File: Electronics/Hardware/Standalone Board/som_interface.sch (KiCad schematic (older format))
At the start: 1 part, among them J1 2309411-2

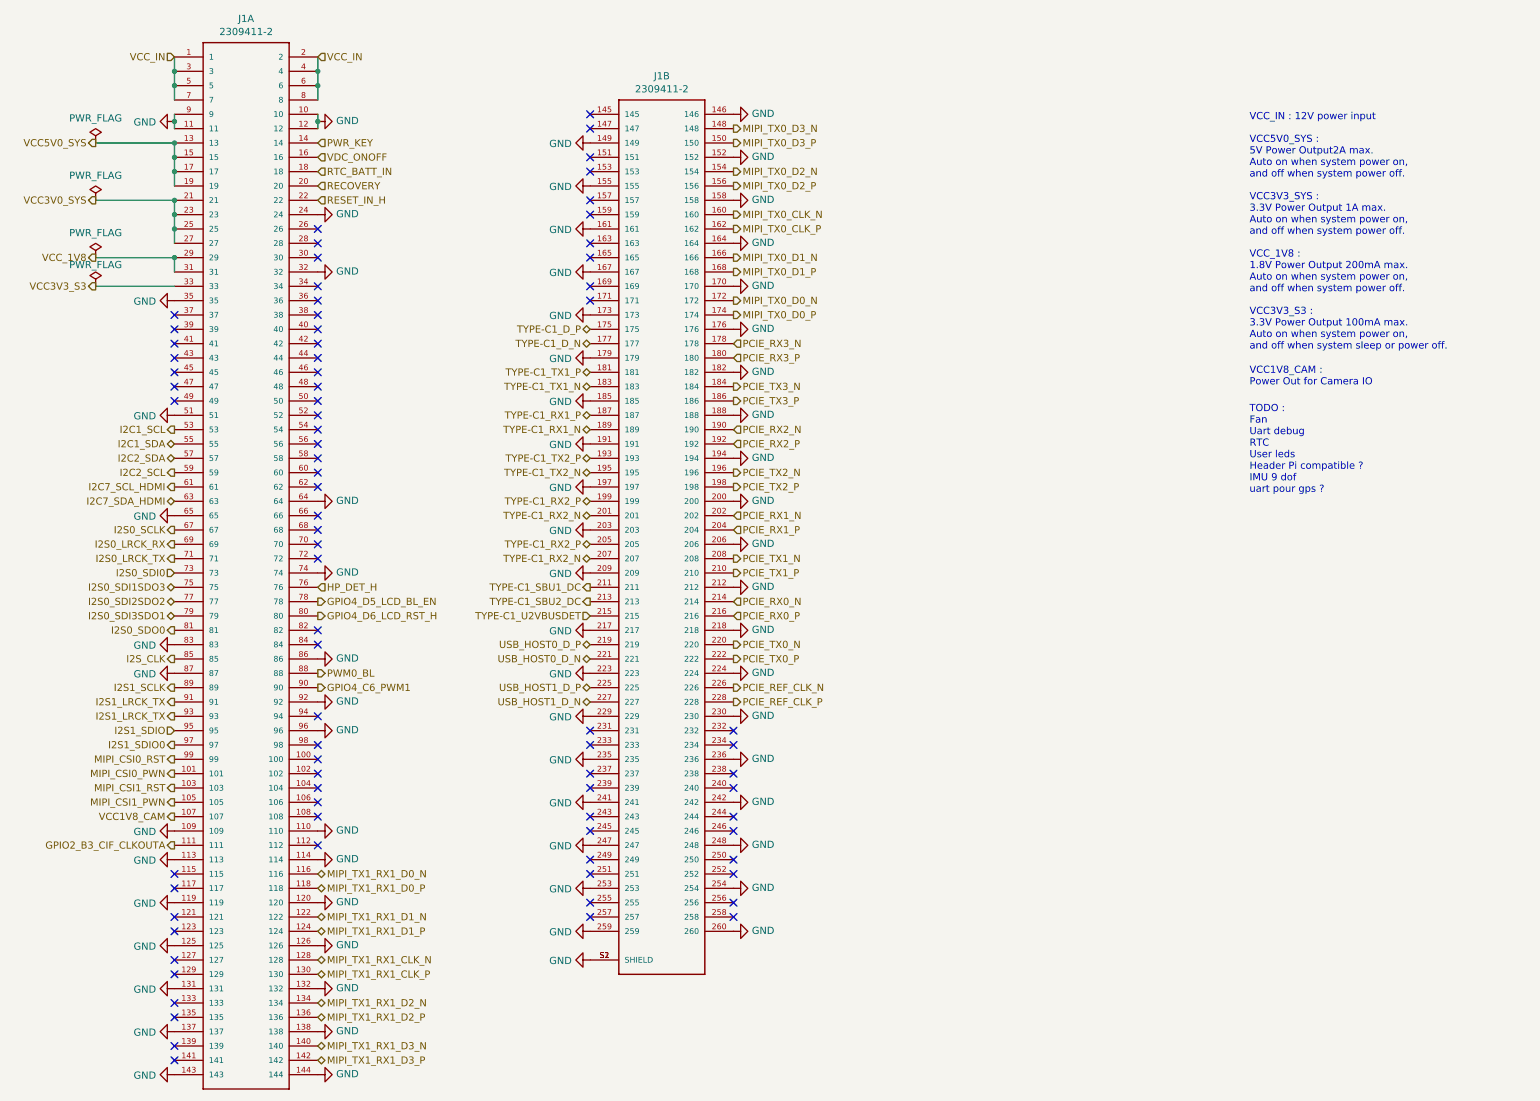
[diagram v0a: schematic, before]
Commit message: Add debug uart, gps uart, fan control and sdcard
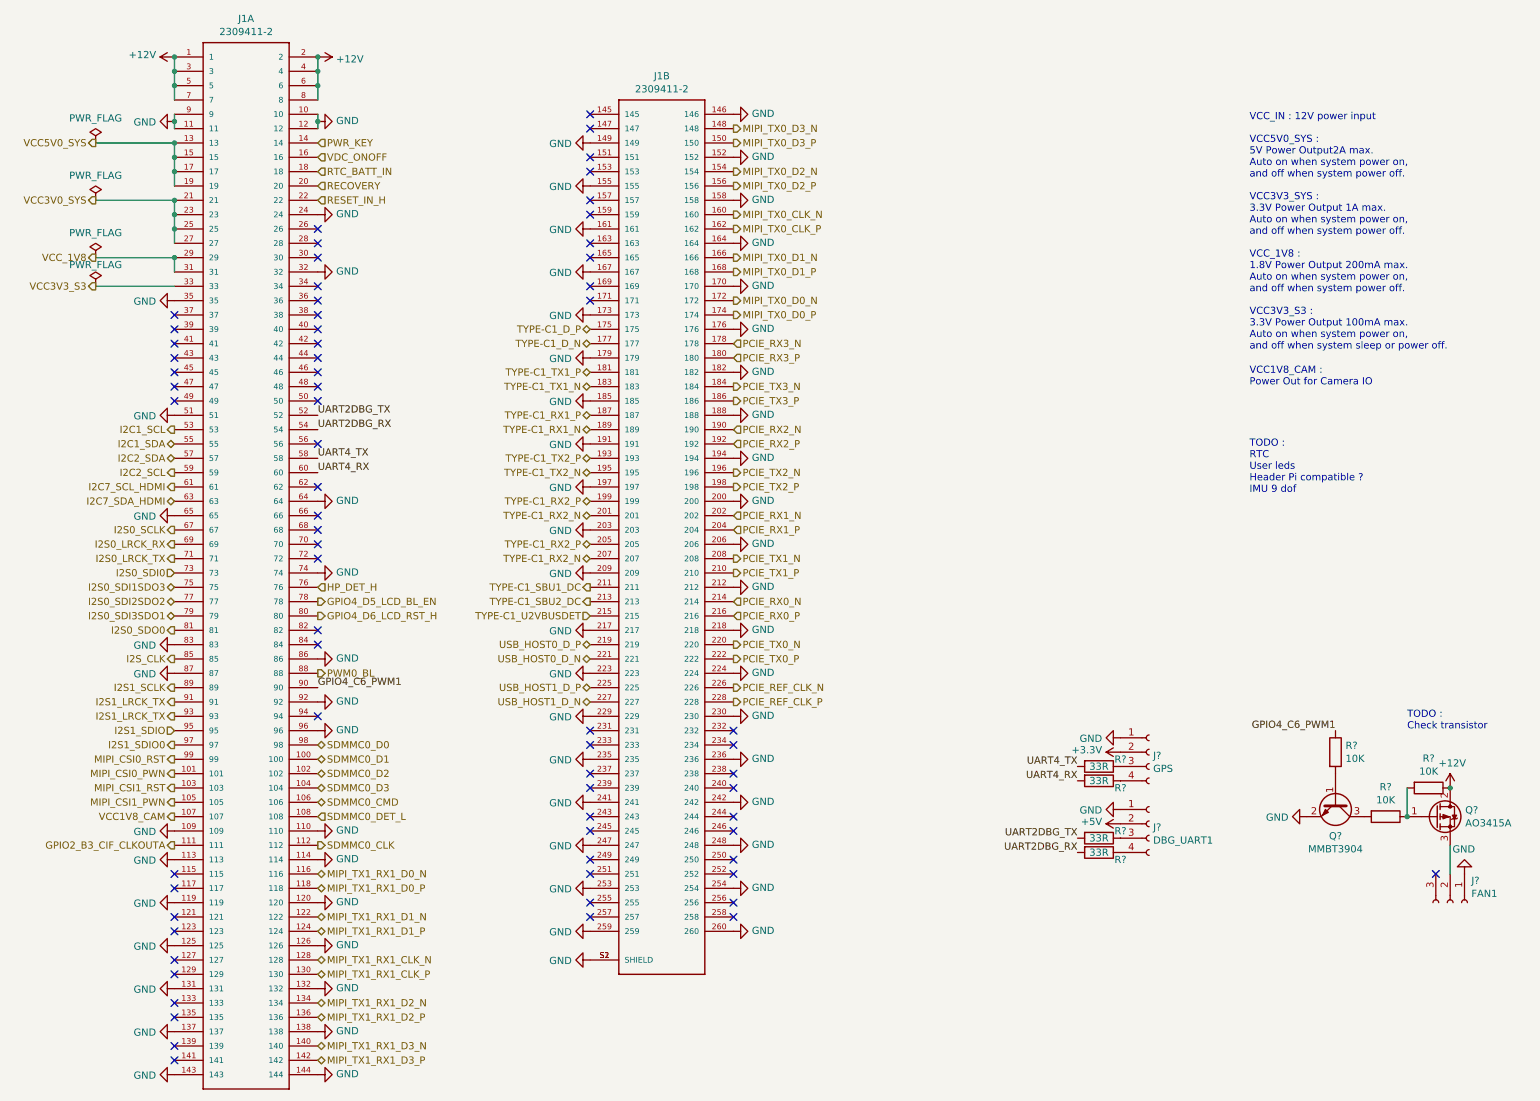
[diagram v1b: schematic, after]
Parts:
- added J?: FAN1, symbol Connector:Conn_01x03_Female
- added J?: DBG_UART1, symbol Connector:Conn_01x04_Female
- added J?: GPS, symbol Connector:Conn_01x04_Female
- added Q?: AO3415A, symbol Device:Q_PMOS_GDS
- added Q?: MMBT3904, Package_TO_SOT_SMD:SOT-23, symbol Transistor_BJT:MMBT3904
- added R? (x3): 10K, symbol Device:R
- added R? (x4): 33R, symbol Device:R
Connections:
- net GND: now also J?.1 (Pin_1), J?.1 (Pin_1), J?.1 (Pin_1), Q?.2 (E)
- net GPIO4_C6_PWM1: now also R?.1
- net SDMMC0_D1: now reaches J1.100
- net SDMMC0_D2: now reaches J1.102
- net SDMMC0_D3: now reaches J1.104
- net SDMMC0_CMD: now reaches J1.106
- net SDMMC0_DET_L: now reaches J1.108
- net SDMMC0_CLK: now reaches J1.112
- net UART2DBG_TX: now reaches J1.52
- net UART2DBG_TX: now also R?.2
- net UART2DBG_RX: now reaches J1.54
- net UART2DBG_RX: now also R?.2
- net UART4_TX: now reaches J1.58
- net UART4_TX: now also R?.2
- net UART4_RX: now reaches J1.60
- net UART4_RX: now also R?.2
- net SDMMC0_D0: now reaches J1.98
- net VCC_IN renamed +12V
- net +12V: now also Q?.2 (D), R?.1
- new net: Q?.1 (G), R?.1, R?.2
- new net: J?.2 (Pin_2), Q?.3 (S)
- new net: Q?.1 (B), R?.2
- new net: Q?.3 (C), R?.2
- new net: J?.3 (Pin_3), R?.1 (x2)
- new net: J?.4 (Pin_4), R?.1 (x2)
- new net +3V3: J?.2 (Pin_2)
- new net +5V: J?.2 (Pin_2)
- no-connect marks 79 -> 69
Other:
- note added: "TODO : \nCheck transistor"
- note added: "TODO :\nRTC\nUser leds\nHeader Pi compatible ?\nIMU 9 dof"
- note removed: "TODO :\nFan\nUart debug\nRTC\nUser leds\nHeader Pi compatible ?\nIMU 9 dof\nuart pour gps ?"

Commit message: Add rtc, pcie + mipi dsi high level connection, usb 2.0, usb 3.0 and remove audio section
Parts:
- added BT?: Battery_Cell, symbol Device:Battery_Cell
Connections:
- net GND: now also BT?.2 (-)
- net RTC_BATT_IN: now also BT?.1 (+)
- net I2C7_SCL_HDMI: no longer names the net of J1.61
- net I2C7_SDA_HDMI: no longer names the net of J1.63
- no-connect marks 69 -> 71
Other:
- note added: "TODO :\nUser leds\nHeader Pi compatible ?\nIMU 9 dof"
- note removed: "TODO :\nRTC\nUser leds\nHeader Pi compatible ?\nIMU 9 dof"
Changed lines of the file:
@@
 EESchema Schematic File Version 4
-LIBS:Standalone Board-cache
 EELAYER 30 0
 EELAYER END
 $Descr A4 11693 8268
 encoding utf-8
-Sheet 2 7
+Sheet 2 6
 Title ""
 Date ""
@@
 Text HLabel 1800 3400 0    50   BiDi ~ 0
 I2C2_SDA
-Text HLabel 1800 3600 0    50   Output ~ 0
-I2C7_SCL_HDMI
-Text HLabel 1800 3700 0    50   BiDi ~ 0
-I2C7_SDA_HDMI
 $Comp
 L power:GND #PWR?
@@
 Text HLabel 2800 1300 2    50   Input ~ 0
 VDC_ONOFF
-Text HLabel 2800 1400 2    50   Input ~ 0
-RTC_BATT_IN
 Text HLabel 2800 1500 2    50   Input ~ 0
 RECOVERY
@@
 NoConn ~ 2800 5200
 Text Notes 9300 3650 0    50   ~ 0
-TODO :\nRTC\nUser leds\nHeader Pi compatible ?\nIMU 9 dof
+TODO :\nUser leds\nHeader Pi compatible ?\nIMU 9 dof
 NoConn ~ 2800 1800
 NoConn ~ 2800 1900
@@
 Text HLabel 2800 6100 2    50   Output ~ 0
 SDMMC0_CLK
+NoConn ~ 1800 3600
+NoConn ~ 1800 3700
+Text Label 2800 1400 0    50   ~ 0
+RTC_BATT_IN
+Text Label 10550 4300 2    50   ~ 0
+RTC_BATT_IN
+$Comp
+L Device:Battery_Cell BT?
+U 1 1 5DF5D410
+P 10550 4500
+F 0 "BT?" H 10668 4596 50  0000 L CNN
+F 1 "Battery_Cell" H 10668 4505 50  0000 L CNN
+F 2 "" V 10550 4560 50  0001 C CNN
+F 3 "~" V 10550 4560 50  0001 C CNN
+	1    10550 4500
+	1    0    0    -1
+$EndComp
+$Comp
+L power:GND #PWR?
+U 1 1 5DF698CD
+P 10550 4600
+F 0 "#PWR?" H 10550 4350 50  0001 C CNN
+F 1 "GND" H 10555 4427 50  0000 C CNN
+F 2 "" H 10550 4600 50  0001 C CNN
+F 3 "" H 10550 4600 50  0001 C CNN
+	1    10550 4600
+	1    0    0    -1
+$EndComp
 $EndSCHEMATC

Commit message: Fix all i2c voltage, add power/reset/recovery button, Mipi dsi hig level, add 3.0/3.3/5/1.1 volt power rail
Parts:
- removed J?: GPS, symbol Connector:Conn_01x04_Female
- removed R? (x2): 33R, symbol Device:R
- added J?: GPIO, symbol Connector:Conn_01x12_Female
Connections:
- net +3V3: now also J?.4 (Pin_4)
- net +5V: now also J?.2 (Pin_2)
- net GND: now also J?.1 (Pin_1), J?.3 (Pin_3)
- net UART4_RX: now also J?.6 (Pin_6)
- net UART4_TX: now also J?.5 (Pin_5)
- net GPIO2_A2: now reaches J1.39
- net GPIO2_A3: now reaches J1.41
- net GPIO1_C2: now reaches J1.42
- net GPIO1_C2: now also J?.9 (Pin_9)
- net GPIO1_C6: now reaches J1.44
- net GPIO1_C6: now also J?.10 (Pin_10)
- net GPIO1_C7: now reaches J1.46
- net GPIO1_C7: now also J?.11 (Pin_11)
- net GPIO1_D0: now reaches J1.48
- net GPIO1_D0: now also J?.12 (Pin_12)
- net GPIO4_C1_I2C3_SCL: now reaches J1.66
- net GPIO4_C1_I2C3_SCL: now also J?.7 (Pin_7)
- net GPIO4_C0_I2C3_SDA: now reaches J1.68
- net GPIO4_C0_I2C3_SDA: now also J?.8 (Pin_8)
- net VCC3V0_SD: now reaches J1.94
- net VCC3V0_SYS renamed VCC3V3_SYS
- no-connect marks 71 -> 62
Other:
- note added: "TODO :\nUser leds"
- note removed: "TODO :\nUser leds\nHeader Pi compatible ?\nIMU 9 dof"
- moved on the sheet: BT?, J?, Q?, R?

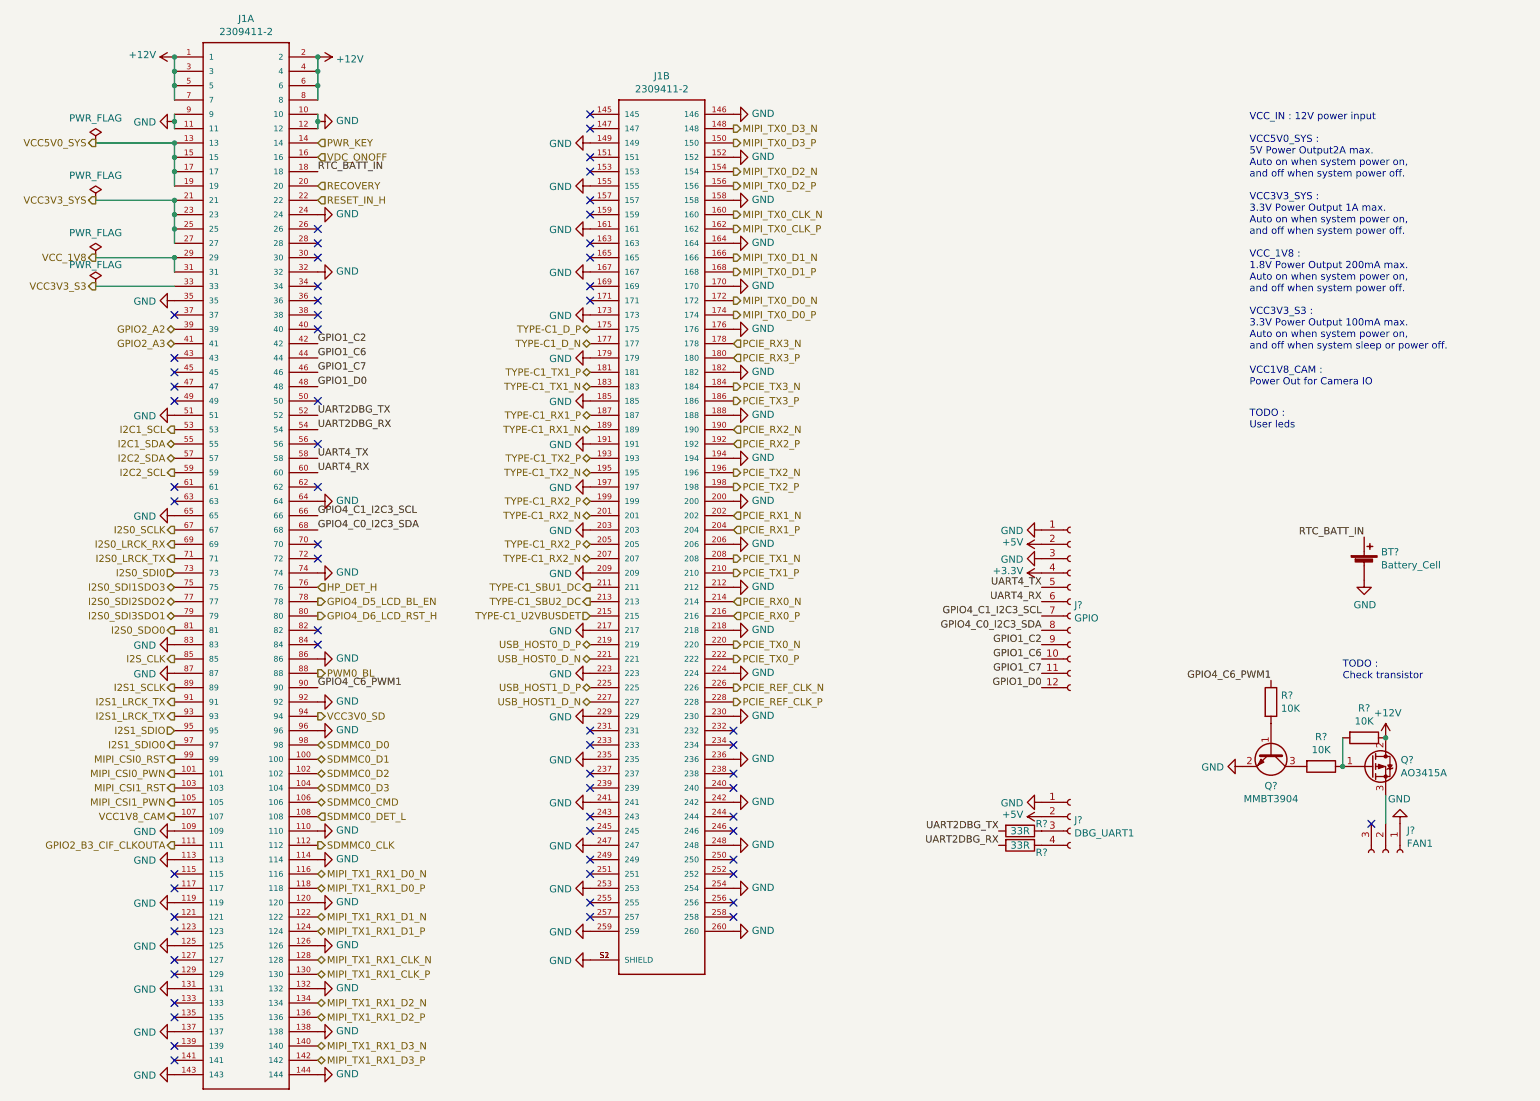
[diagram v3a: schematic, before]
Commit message: Everything is routed, TODO : lenghtmatching + impedance matching + cleaning
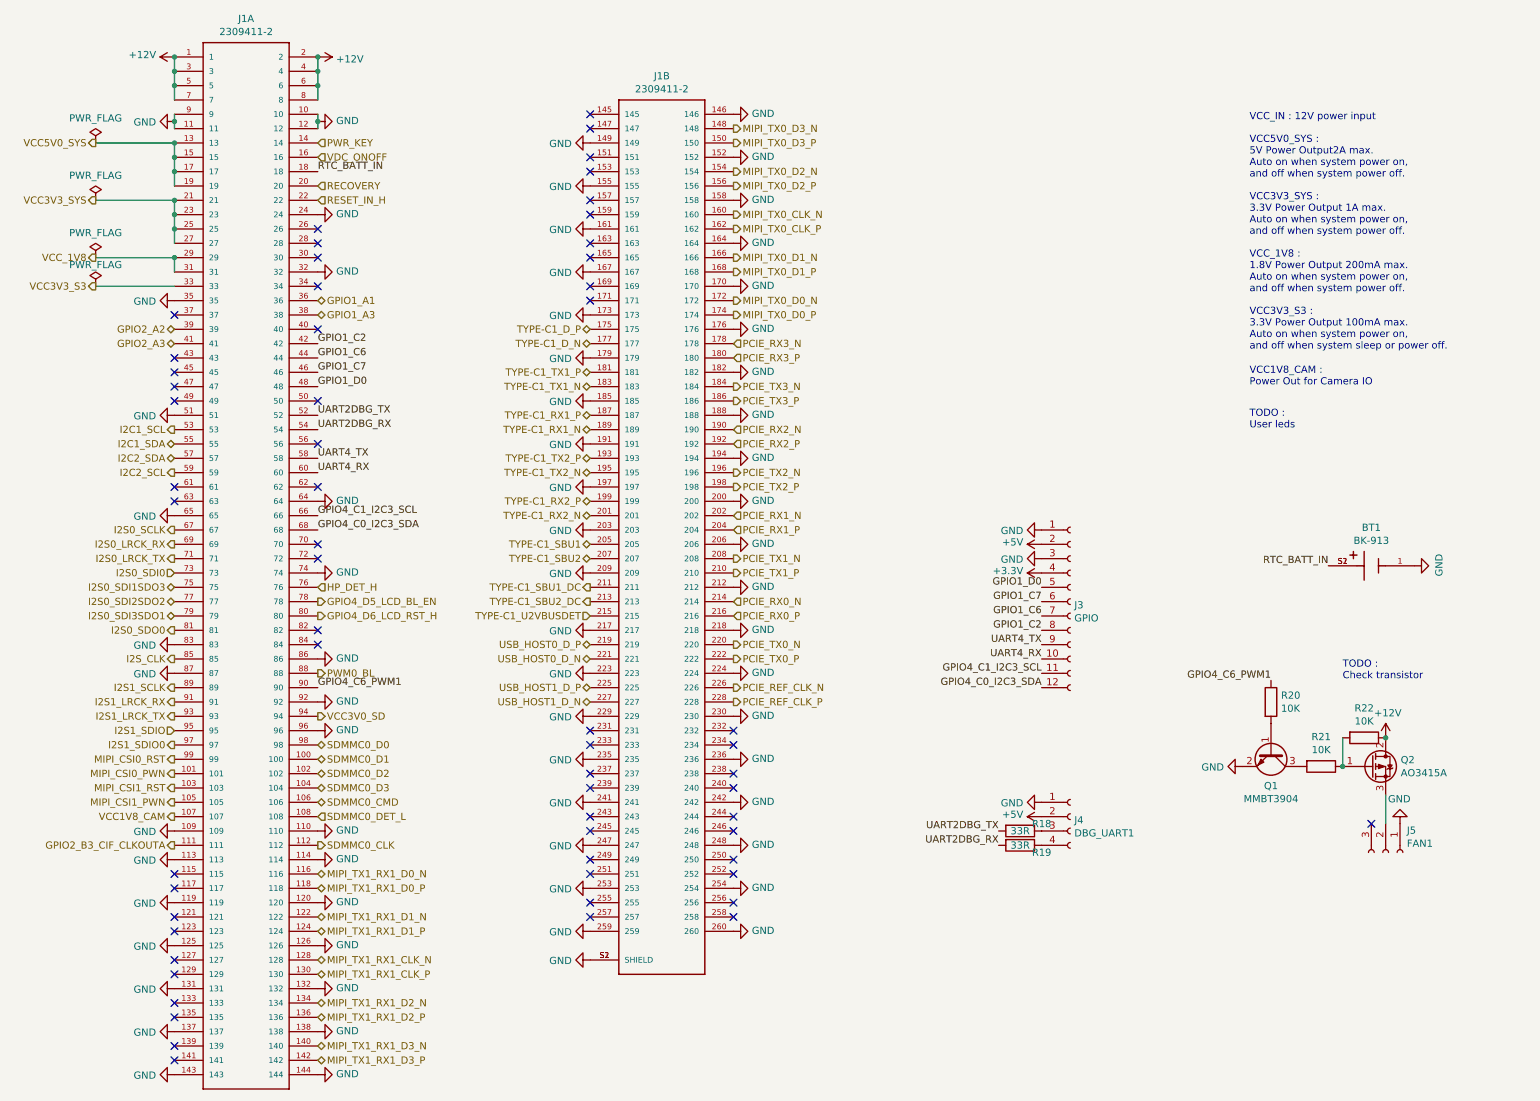
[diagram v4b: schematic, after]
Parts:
- removed BT?: Battery_Cell, symbol Device:Battery_Cell
- added BT1: BK-913, BK-913:BAT_BK-913, symbol BK-913:BK-913
- J3: renamed from J?; footprint (none) -> Connector_PinHeader_1.00mm:PinHeader_1x12_P1.00mm_Vertical
- J4: renamed from J?; footprint (none) -> Connector_PinHeader_1.00mm:PinHeader_1x04_P1.00mm_Vertical
- J5: renamed from J?; footprint (none) -> Connector_PinHeader_1.00mm:PinHeader_1x03_P1.00mm_Vertical
- Q2: renamed from Q?; footprint (none) -> Package_TO_SOT_SMD:SOT-23
- R18, R19, R20, R21, R22: renamed from R?; footprint (none) -> Resistor_SMD:R_0201_0603Metric
- gave numbers to parts that had none: 1
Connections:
- net GND: now also BT1.1 (-)
- net GPIO1_C2: now also J3.8 (Pin_8); no longer J3.9 (Pin_9)
- net GPIO1_C6: now also J3.7 (Pin_7); no longer J3.10 (Pin_10)
- net GPIO1_C7: now also J3.6 (Pin_6); no longer J3.11 (Pin_11)
- net GPIO1_D0: now also J3.5 (Pin_5); no longer J3.12 (Pin_12)
- net GPIO4_C0_I2C3_SDA: now also J3.12 (Pin_12); no longer J3.8 (Pin_8)
- net GPIO4_C1_I2C3_SCL: now also J3.11 (Pin_11); no longer J3.7 (Pin_7)
- net I2S1_LRCK_TX: no longer J1.91
- net RTC_BATT_IN: now also BT1.S1 (+), BT1.S2 (+)
- net TYPE-C1_RX2_N: no longer J1.207
- net TYPE-C1_RX2_P: no longer J1.205
- net UART4_RX: now also J3.10 (Pin_10); no longer J3.6 (Pin_6)
- net UART4_TX: now also J3.9 (Pin_9); no longer J3.5 (Pin_5)
- net GPIO1_A1: now reaches J1.36
- net GPIO1_A3: now reaches J1.38
- new net I2S1_LRCK_RX: J1.91
- new net TYPE-C1_SBU1: J1.205
- new net TYPE-C1_SBU2: J1.207
- no-connect marks 62 -> 60
